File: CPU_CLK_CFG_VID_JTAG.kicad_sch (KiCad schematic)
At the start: 1 part

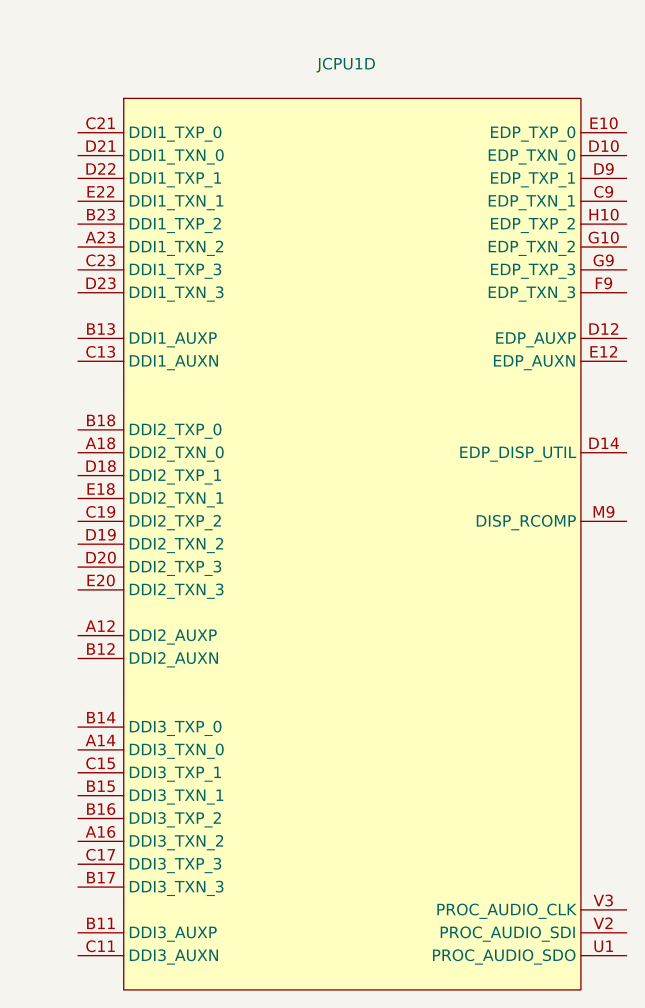
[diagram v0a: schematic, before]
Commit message: Added CPU clock/cfg/vid/jtag symbol
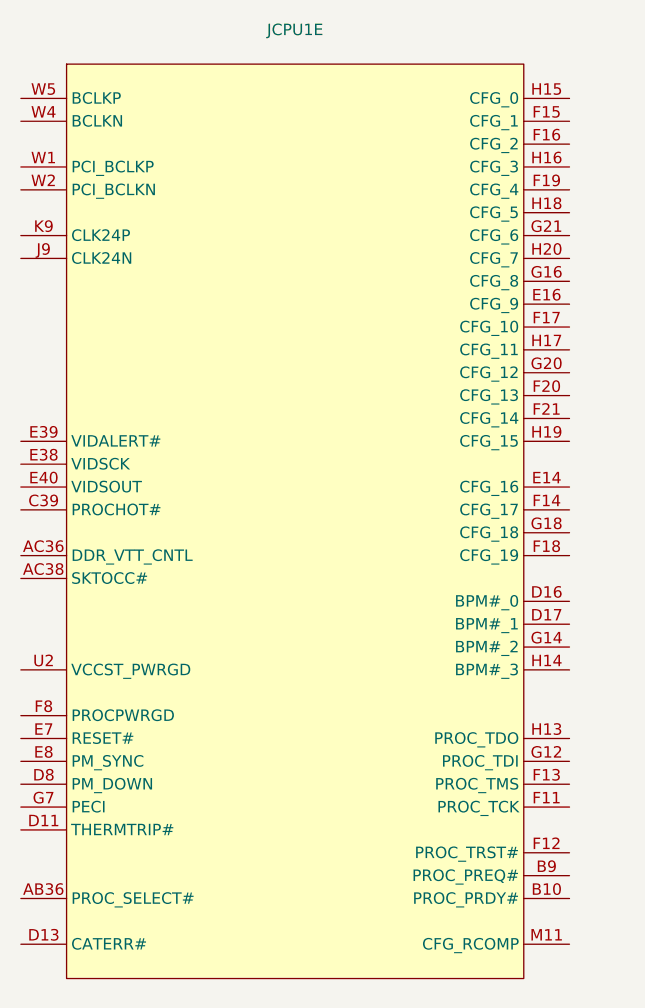
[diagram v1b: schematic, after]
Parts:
- removed JCPU1: ~, A-my-stuff:LGA-1151_L47.1-W42.5-P0.91_PE115127-4041-01H, symbol A-my-stuff:Intel_CFL_1151
- added JCPU1: ~, A-my-stuff:LGA-1151_L47.1-W42.5-P0.91_PE115127-4041-01H, symbol A-my-stuff:Intel_CFL_1151
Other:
- title: CPU Display outputs -> CPU Clock, CFG, VID & JTAG
